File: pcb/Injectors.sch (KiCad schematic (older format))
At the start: 48 parts, among them Q1 VND14NV04, Q2 VND14NV04, Q3 VND14NV04, Q4 VND14NV04, Q5 VND14NV04, Q6 VND14NV04, Q7 VND14NV04, Q8 VND14NV04

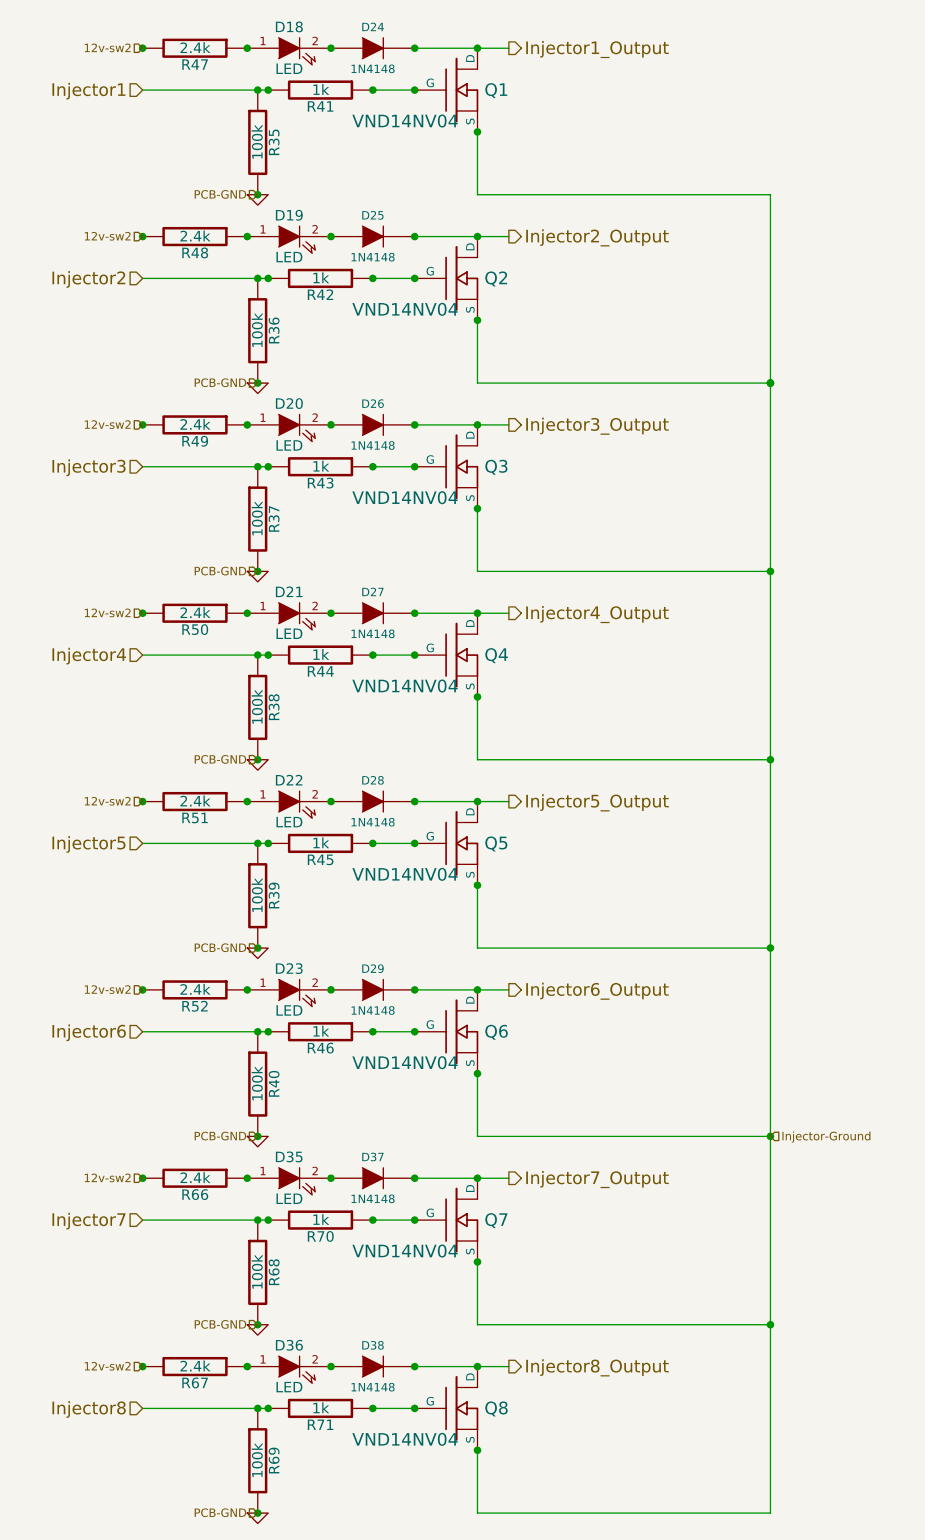
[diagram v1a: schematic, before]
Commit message: Added additional wire connection points for 1 ground connection per Injector MOSFET and increased the size of the trace to these pads
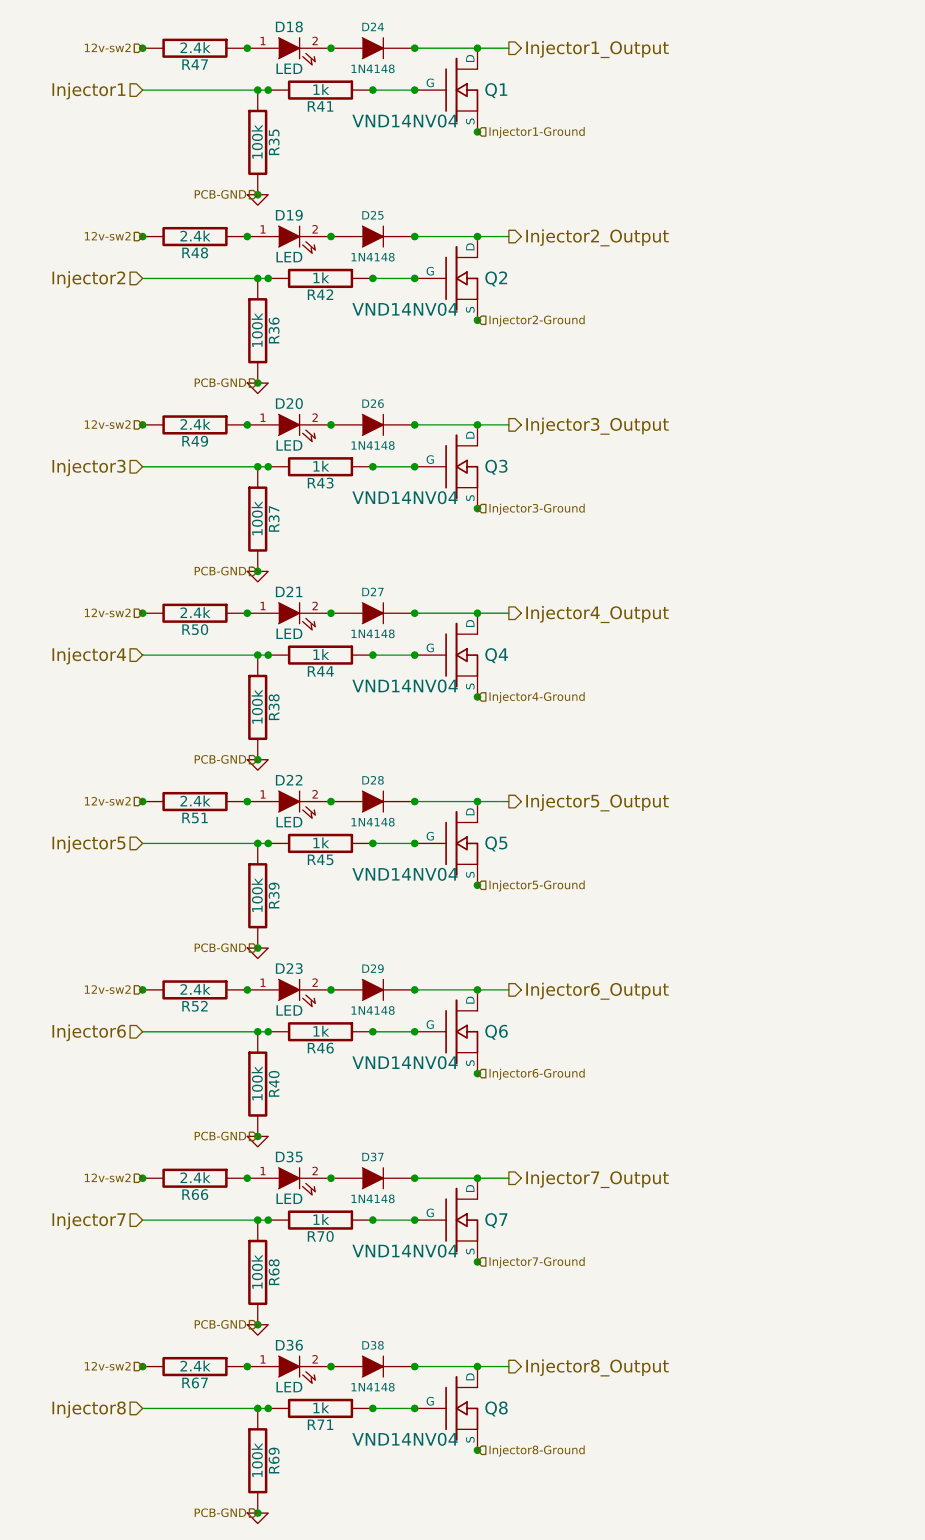
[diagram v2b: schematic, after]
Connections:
- removed net Injector-Ground: Q1.S, Q2.S, Q3.S, Q4.S, Q5.S, Q6.S, Q7.S, Q8.S
- new net Injector1-Ground: Q1.S
- new net Injector2-Ground: Q2.S
- new net Injector3-Ground: Q3.S
- new net Injector4-Ground: Q4.S
- new net Injector5-Ground: Q5.S
- new net Injector6-Ground: Q6.S
- new net Injector7-Ground: Q7.S
- new net Injector8-Ground: Q8.S
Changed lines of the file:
@@
-EESchema Schematic File Version 2  date Thu 05 Jul 2012 11:32:25 AM EDT
+EESchema Schematic File Version 2  date Fri 06 Jul 2012 12:40:00 PM EDT
 LIBS:opto
 LIBS:Jaguar
@@
 Sheet 6 7
 Title "Jaguar PCB for FreeEMS"
-Date "5 jul 2012"
+Date "6 jul 2012"
 Rev "A4"
 Comp "diyefi.org"
@@
 Comment4 ""
 $EndDescr
+Text HLabel 4000 7400 2    40   Input ~ 0
+Injector8-Ground
+Text HLabel 4000 6500 2    40   Input ~ 0
+Injector7-Ground
+Text HLabel 4000 4700 2    40   Input ~ 0
+Injector5-Ground
+Text HLabel 4000 5600 2    40   Input ~ 0
+Injector6-Ground
+Text HLabel 4000 3800 2    40   Input ~ 0
+Injector4-Ground
+Text HLabel 4000 2900 2    40   Input ~ 0
+Injector3-Ground
+Text HLabel 4000 2000 2    40   Input ~ 0
+Injector2-Ground
+Text HLabel 4000 1100 2    40   Input ~ 0
+Injector1-Ground
 Text HLabel 2950 7700 0    40   Input ~ 0
 PCB-GND
@@
 $EndComp
 Wire Wire Line
-	5400 7700 4000 7700
-Wire Wire Line
-	5400 5900 4000 5900
-Wire Wire Line
-	4000 4700 4000 5000
-Wire Wire Line
-	5400 4100 4000 4100
-Wire Wire Line
-	5400 2300 4000 2300
-Connection ~ 5400 2300
-Connection ~ 5400 6800
-Wire Wire Line
-	5400 7700 5400 1400
-Wire Wire Line
 	3700 1600 4150 1600
 Wire Wire Line
@@
 Connection ~ 2400 3400
 Connection ~ 2400 4300
-Connection ~ 5400 2300
-Connection ~ 5400 4100
 Wire Wire Line
 	2400 5400 3000 5400
 Connection ~ 2400 5200
-Connection ~ 5400 5900
 Connection ~ 3700 1600
 Connection ~ 3700 700
@@
 Connection ~ 2900 700
 Connection ~ 3300 700
-Wire Wire Line
-	4000 1100 4000 1400
 Connection ~ 2950 1400
 Wire Wire Line
@@
 	3700 1800 3500 1800
 Connection ~ 2950 2300
-Wire Wire Line
-	4000 2300 4000 2000
 Connection ~ 2950 2700
 Connection ~ 3000 2700
@@
 	3700 2700 3500 2700
 Connection ~ 2950 3200
-Wire Wire Line
-	4000 2900 4000 3200
 Connection ~ 2950 3600
 Connection ~ 3000 3600
@@
 	3700 3600 3500 3600
 Connection ~ 2950 4100
-Wire Wire Line
-	4000 4100 4000 3800
 Connection ~ 2950 5000
 Wire Wire Line
@@
 	3700 5400 3500 5400
 Connection ~ 2950 5900
-Wire Wire Line
-	4000 5900 4000 5600
 Connection ~ 4000 700
 Wire Wire Line
 	3000 4500 2400 4500
-Connection ~ 5400 5000
-Connection ~ 5400 3200
 Wire Wire Line
 	2400 3600 3000 3600
@@
 	3000 1800 2400 1800
 Connection ~ 3700 6100
-Wire Wire Line
-	4000 6500 4000 6800
 Connection ~ 2950 6800
 Wire Wire Line
@@
 	3700 7200 3500 7200
 Connection ~ 2950 7700
-Wire Wire Line
-	4000 7700 4000 7400
 Connection ~ 3700 7000
-Wire Wire Line
-	4000 1400 5400 1400
-Wire Wire Line
-	4000 3200 5400 3200
-Wire Wire Line
-	4000 5000 5400 5000
-Wire Wire Line
-	4000 6800 5400 6800
 $Comp
 L GND #PWR039
@@
 Text HLabel 2400 1600 0    40   Input ~ 0
 12v-sw2
-Text HLabel 5400 5900 2    40   Input ~ 0
-Injector-Ground
 Text HLabel 2400 2700 0    60   Input ~ 0
 Injector3
